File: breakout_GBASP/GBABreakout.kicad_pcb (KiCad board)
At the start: 2 copper layers, 19.9 x 10 mm, 17 parts, among them J1 Conn_01x16, J10 TP8, J11 TP3, J12 TP2, J13 S02, J14 S01, J15 CK1, J16 EX1, J17 GND, J2 VCC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

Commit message: some minor changes
* improved SP compatibility
* changed via diameter to 0.6mm and holesize to 0.3mm
* updated Readme
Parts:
- J1: footprint OFFSET:JUSHUO_AFC07-S16FCC-00 -> Connector_FFC-FPC:TE_1-1734839-6_1x16-1MP_P0.5mm_Horizontal
- J16: value EX1 -> BAT+
- moved J1 0.42 mm to (180.8, 60.4)
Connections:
- net EXTRA1 renamed BAT+
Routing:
- net GND: vias 7 -> 5

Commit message: updated shield
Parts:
- J16: value BAT+ -> EX1
- moved J2 9.52 mm to (177.0, 66.3), turned to 180 degrees
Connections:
- net BAT+ renamed EX1
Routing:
- net GBA_VCC: track 5.46 -> 13.2 mm, vias 0 -> 2
- net EX1: track 10.9 -> 12.3 mm
- net GBA_L: track 14.5 -> 15.2 mm
- net GND: track 2.75 -> 2.51 mm, vias 5 -> 4

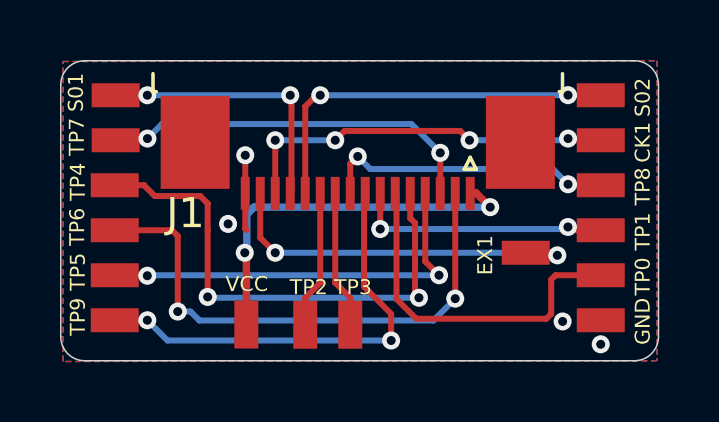
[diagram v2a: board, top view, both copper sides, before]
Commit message: Updated files to KiCad6
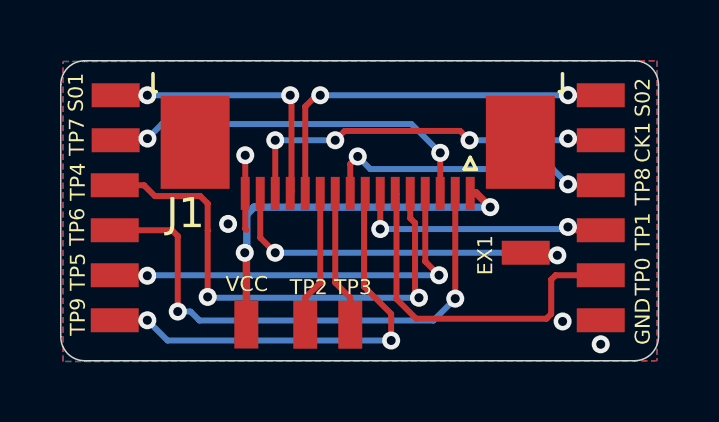
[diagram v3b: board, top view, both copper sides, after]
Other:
- net class Default removed
- net class PWR removed
